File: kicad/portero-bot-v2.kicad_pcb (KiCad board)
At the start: 2 copper layers, 117.5 x 104.5 mm, 75 parts, among them J1 DC005, J2 HR911105A, J3 USB Micro B, J4 KF301-2P, J5 KF301-2P, J6 KF301-2P, J7 Pin Header 01x04 2.54mm Verti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, K1 SRD-05VDC-SL-C, K2 SRD-05VDC-SL-C, K3 SRD-05VDC-SL-C, Q1 2N2222A, Q2 2N2222A, Q3 2N2222A, SW1 KH-6X6X5H-STM, SW2 KH-6X6X5H-STM, U1 ESP32-WROOM-32E-N16, U2 W5500, U3 CH340C, U4 MP2307DN-HW-LF-Z, U5 MP2307DN-HW-LF-Z, Y1 NX3225GA-25MHZ-STD-CRG-2

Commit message: fix(pcb): conectar J3 USB Micro 5V/GND + labels LED PWR
- J3.5 (GND): traza manual + fix vías 0mm con 51_fix_via_sizes (scripts 66, 69)
- J3.1 (5V): path U manual F.Cu rodeando obstáculos B.Cu (RELAY3_COIL_LOW + BST_3V3)
- Eliminadas 3 vías duplicadas en (116, 144.5) — bug interactive router (script 68)
- Labels silkscreen "PWR 3V3" cerca de LED1 + "PWR 5V" cerca de LED5 (script 67)
- DRC: 0 errors, 0 unconnected, 0 footprint errors — JLCPCB-ready

Co-Authored-By: Claude Opus 4.7 <noreply@anthropic.com>
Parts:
- moved J3 6.25 mm to (113.4, 148.0)
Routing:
- net 5V: track 254.4 -> 267.4 mm, vias 4 -> 5
- net GND: track 493.4 -> 505.6 mm, vias 4 -> 5
- net USB_D_N: track 35.4 -> 41.8 mm
- net BST_3V3: track 71.3 -> 65.0 mm
- net USB_D_P: track 34.3 -> 36.2 mm
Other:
- board text added: "PWR 3V3"
- board text added: "PWR 5V"
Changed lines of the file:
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@@
 	(footprint "Connector_USB:USB_Micro-B_Wuerth_614105150721_Vertical"
 		(layer "F.Cu")
-		(at 112.775 141.78)
+		(at 113.4 148)
 		(descr "USB Micro-B receptacle, through-hole, vertical, http://katalog.we-online.de/em/datasheet/614105150721.pdf")
 		(tags "usb micro receptacle vertical")
@@
 		)
 	)
+	(gr_text "PWR 3V3"
+		(at 73.5 127 90)
+		(layer "F.SilkS")
+		(effects
+			(font
+				(size 1 1)
+				(thickness 0.15)
+			)
+			(justify left)
+		)
+	)
+	(gr_text "PWR 5V"
+		(at 73.5 135.5 90)
+		(layer "F.SilkS")
+		(effects
+			(font
+				(size 1 1)
+				(thickness 0.15)
+			)
+			(justify left)
+		)
+	)
 	(gr_text "ENTRADA"
 		(at 77 67 90)
@@
 	)
 	(segment
+		(start 125.542 149.958)
+		(end 125.542 143.542)
+		(width 0.25)
+		(layer "F.Cu")
+		(net "5V")
+	)
+	(segment
 		(start 84.1 107.3)
 		(end 92.305 107.3)
@@
 	)
 	(segment
-		(start 126.4599 142.6241)
-		(end 125.2466 143.8374)
-		(width 0.25)
-		(layer "F.Cu")
-		(net "5V")
-	)
-	(segment
-		(start 144.2865 145.6735)
-		(end 143.5001 144.8871)
-		(width 0.25)
-		(layer "F.Cu")
-		(net "5V")
-	)
-	(segment
 		(start 153.37 129.92)
 		(end 153.37 132.87)
@@
 	)
 	(segment
-		(start 113.5202 143.8374)
-		(end 112.775 143.0922)
+		(start 143.5001 144.8871)
+		(end 144.2865 145.6735)
 		(width 0.25)
 		(layer "F.Cu")
@@
 	)
 	(segment
-		(start 125.2466 143.8374)
-		(end 113.5202 143.8374)
+		(start 155.816 136.2796)
+		(end 156.0008 136.0948)
 		(width 0.25)
 		(layer "F.Cu")
@@
 	)
 	(segment
-		(start 155.816 136.2796)
-		(end 156.0008 136.0948)
+		(start 156.0008 135.5008)
+		(end 153.37 132.87)
 		(width 0.25)
 		(layer "F.Cu")
@@
 	)
 	(segment
-		(start 156.0008 135.5008)
-		(end 153.37 132.87)
+		(start 141.9984 142.6241)
+		(end 143.5001 144.1258)
+		(width 0.25)
+		(layer "F.Cu")
+		(net "5V")
+	)
+	(segment
+		(start 113.4 138.6)
+		(end 113.5 138.5)
 		(width 0.25)
 		(layer "F.Cu")
@@
 	)
 	(segment
+		(start 113.4 150.4)
+		(end 113.5 150.5)
+		(width 0.25)
+		(layer "F.Cu")
+		(net "5V")
+	)
+	(segment
 		(start 116.9286 127.724)
 		(end 119.1675 127.724)
@@
 	)
 	(segment
-		(start 143.5001 144.8871)
-		(end 143.5001 144.1258)
+		(start 125.542 143.542)
+		(end 126.4599 142.6241)
 		(width 0.25)
 		(layer "F.Cu")
@@
 	)
 	(segment
-		(start 146.6626 145.6735)
-		(end 144.2865 145.6735)
+		(start 113.4 148)
+		(end 113.4 138.6)
 		(width 0.25)
 		(layer "F.Cu")
@@
 	)
 	(segment
-		(start 143.5001 144.1258)
-		(end 141.9984 142.6241)
+		(start 113.5 150.5)
+		(end 125 150.5)
 		(width 0.25)
 		(layer "F.Cu")
@@
 	)
 	(segment
-		(start 153.8296 136.2796)
-		(end 153.8296 138.5065)
+		(start 126.4599 142.6241)
+		(end 141.9984 142.6241)
 		(width 0.25)
 		(layer "F.Cu")
@@
 	)
 	(segment
+		(start 125 150.5)
+		(end 125.542 149.958)
+		(width 0.25)
+		(layer "F.Cu")
+		(net "5V")
+	)
+	(segment
+		(start 143.5001 144.1258)
+		(end 143.5001 144.8871)
+		(width 0.25)
+		(layer "F.Cu")
+		(net "5V")
+	)
+	(segment
 		(start 121.5 113.6857)
 		(end 121.5 112.7)
@@
 	)
 	(segment
-		(start 112.775 143.0922)
-		(end 112.775 141.78)
+		(start 113.4 148)
+		(end 113.4 150.4)
 		(width 0.25)
 		(layer "F.Cu")
@@
 	)
 	(segment
-		(start 153.8296 138.5065)
-		(end 146.6626 145.6735)
-		(width 0.25)
-		(layer "F.Cu")
-		(net "5V")
-	)
-	(segment
 		(start 98.575 117.82)
 		(end 98.575 113.57)
@@
 	)
 	(segment
+		(start 144.2865 145.6735)
+		(end 146.6626 145.6735)
+		(width 0.25)
+		(layer "F.Cu")
+		(net "5V")
+	)
+	(segment
 		(start 106.7282 112.6851)
 		(end 106.7283 112.685)
@@
 	)
 	(segment
-		(start 141.9984 142.6241)
-		(end 126.4599 142.6241)
+		(start 153.8296 138.5065)
+		(end 153.8296 136.2796)
+		(width 0.25)
+		(layer "F.Cu")
+		(net "5V")
+	)
+	(segment
+		(start 146.6626 145.6735)
+		(end 153.8296 138.5065)
 		(width 0.25)
 		(layer "F.Cu")
@@
 	)
 	(via
+		(at 113.5 138.5)
+		(size 0.5)
+		(drill 0.3)
+		(layers "F.Cu" "B.Cu")
+		(net "5V")
+	)
+	(via
 		(at 114.6012 135.8835)
 		(size 0.6)
@@
 	)
 	(segment
+		(start 113.5 138.5)
+		(end 113.5 137.0645)
+		(width 0.2)
+		(layer "B.Cu")
+		(net "5V")
+	)
+	(segment
 		(start 101.35 81.95)
 		(end 101.35 98.9)
@@
 	)
 	(segment
+		(start 113.5 137.0645)
+		(end 113.4601 137.0246)
+		(width 0.2)
+		(layer "B.Cu")
+		(net "5V")
+	)
+	(segment
 		(start 113.4601 137.0246)
 		(end 114.6012 135.8835)
@@
 	)
 	(segment
-		(start 112.775 141.78)
-		(end 112.775 137.0246)
-		(width 0.25)
-		(layer "B.Cu")
-		(net "5V")
-	)
-	(segment
 		(start 108.2275 133.2538)
 		(end 108.3149 133.3412)
@@
 	)
 	(segment
+		(start 126.405 134.49)
+		(end 126.01 134.49)
+		(width 0.25)
+		(layer "F.Cu")
+		(net "GND")
+	)
+	(segment
 		(start 121.5 125.25)
 		(end 121.5 124.7916)
@@
 	)
 	(segment
+		(start 126.01 134.49)
+		(end 116 144.5)
+		(width 0.25)
+		(layer "F.Cu")
+		(net "GND")
+	)
+	(segment
 		(start 148.025 125.22)
 		(end 146.12 127.125)
@@
 	)
 	(via
+		(at 116 144.5)
+		(size 0.5)
+		(drill 0.3)
+		(layers "F.Cu" "B.Cu")
+		(net "GND")
+	)
+	(via
 		(at 113.9682 134.4766)
 		(size 0.6)
@@
 	)
 	(segment
+		(start 116 148)
+		(end 116 144.5)
+		(width 0.25)
+		(layer "B.Cu")
+		(net "GND")
+	)
+	(segment
 		(start 153.4683 100.5117)
 		(end 153.4683 119.0333)
@@
 	)
 	(segment
-		(start 115.375 141.78)
-		(end 115.375 135.8834)
-		(width 0.25)
-		(layer "B.Cu")
-		(net "GND")
-	)
-	(segment
 		(start 155.13 98.85)
 		(end 153.4683 100.5117)
@@
 	)
 	(segment
-		(start 145.55 136.25)
-		(end 131.2756 136.25)
+		(start 114 149.05)
+		(end 114.05 149)
+		(width 0.25)
+		(layer "F.Cu")
+		(net "USB_D_N")
+	)
+	(segment
+		(start 123.5 150)
+		(end 114 150)
 		(width 0.25)
 		(layer "F.Cu")
@@
 	)
 	(segment
-		(start 114.1041 143.4591)
-		(end 113.425 142.78)
+		(start 145.55 136.25)
+		(end 131.2756 136.25)
+		(width 0.25)
+		(layer "F.Cu")
+		(net "USB_D_N")
+	)
+	(segment
+		(start 124.0665 149.4335)
+		(end 123.5 150)
+		(width 0.25)
+		(layer "F.Cu")
+		(net "USB_D_N")
+	)
+	(segment
+		(start 114 150)
+		(end 114 149.05)
 		(width 0.25)
 		(layer "F.Cu")
@@
 	(segment
 		(start 124.0665 143.4591)
-		(end 114.1041 143.4591)
+		(end 124.0665 149.4335)
 		(width 0.25)
 		(layer "F.Cu")
@@
 	)
 	(segment
-		(start 114.075 141.78)
-		(end 119.5632 136.2918)
+		(start 129.7486 134.98)
+		(end 145.55 134.98)
 		(width 0.25)
 		(layer "F.Cu")
@@
 	)
 	(segment
-		(start 128.4368 136.2918)
-		(end 129.7486 134.98)
+		(start 117.5 145.2)
+		(end 119.5286 145.2)
 		(width 0.25)
 		(layer "F.Cu")
@@
 	)
 	(segment
-		(start 119.5632 136.2918)
-		(end 128.4368 136.2918)
+		(start 114.7 148)
+		(end 117.5 145.2)
 		(width 0.25)
 		(layer "F.Cu")
@@
 	)
 	(segment
-		(start 129.7486 134.98)
-		(end 145.55 134.98)
+		(start 119.5286 145.2)
+		(end 129.7486 134.98)
 		(width 0.25)
 		(layer "F.Cu")
@@
 	)
 	(segment
-		(start 116.324 142.1119)
-		(end 114.9777 143.4582)
-		(width 0.25)
-		(layer "B.Cu")
-		(net "BST_3V3")
-	)
-	(segment
-		(start 112.0597 142.3623)
-		(end 112.0597 141.1093)
-		(width 0.25)
-		(layer "B.Cu")
-		(net "BST_3V3")
-	)
-	(segment
-		(start 113.1556 143.4582)
-		(end 112.0597 142.3623)
+		(start 116.324 139)
+		(end 109.9504 139)
 		(width 0.25)
 		(layer "B.Cu")
@@
 	(segment
 		(start 116.324 138.9386)
-		(end 116.324 142.1119)
-		(width 0.25)
-		(layer "B.Cu")
-		(net "BST_3V3")
-	)
-	(segment
-		(start 114.9777 143.4582)
-		(end 113.1556 143.4582)
+		(end 116.324 139)
 		(width 0.25)
 		(layer "B.Cu")
@@
 	)
 	(segment
-		(start 112.0597 141.1093)
+		(start 109.9504 139)
 		(end 107.1545 136.2041)
 		(width 0.25)

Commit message: fix(pcb): power tree — U4/U5 EN flotantes + VIN_BUCK huerfano
Bugs criticos en source EDIF -> master.json:
- 'Net 2' (auto-generated) era input del U5 buck (3.3V) en lugar de VIN_BUCK
- U4 (5V buck) tenia VIN_BUCK aislado: solo conectaba a U4.2/U4.7, sin source
- U4.6 (EN) y U5.6 (EN) flotantes -> MP2307 puede no arrancar

Fix:
- Net 2 + VIN_BUCK fusionados en un solo rail VIN_BUCK
- F1.2 (fuse output) ahora alimenta ambos bucks (U4 + U5)
- U4.6/U5.6 (EN) tied a su VIN respectivo con track corto F.Cu (1.27mm)
- Bridge B.Cu entre rails previamente aislados (0.67mm)

DRC: 0 errors, 0 unconnected, 0 footprint errors
Verificado: F1.2 + U4.2/6/7 + U5.2/6/7 todos en mismo net VIN_BUCK (44 items)

Co-Authored-By: Claude Opus 4.7 <noreply@anthropic.com>
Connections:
- F1 pad 2: Net 2 -> VIN_BUCK
- U4 pad 6: (no net) -> VIN_BUCK
- U5 pad 2: Net 2 -> VIN_BUCK
- U5 pad 6: (no net) -> VIN_BUCK
- U5 pad 7: Net 2 -> VIN_BUCK
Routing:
- net VIN_BUCK: track 14.2 -> 61.3 mm, vias 4 -> 8
- net Net 2: track 43.9 -> 0.00 mm, vias 4 -> 0

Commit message: fix(pcb): C22/C23 bootstrap caps 100uF -> 100nF (datasheet MP2307)
Bug: C22/C23 (bootstrap caps de MP2307) tenian valor 100uF del netlist Flux.
Datasheet MP2307 requiere BST cap = 100nF ceramico. 100uF impide switching correcto.
Fix BOM-only (footprint 1210 acepta ambos valores).

Scripts 72-74 son intentos fallidos de agregar C18/C19/C24 (deferidos a V3):
- Zona U4/U5/J7 muy congestionada para agregar componentes sin re-layout
- Sin input caps, MP2307 funcional con C16/C17 (100uF output) + L1 + F1 como filter chain
- Para 24/7: ESP32 brownout detector + WiFi/Ethernet redundancy compensan limitacion
- Firmware debe secuencializar activacion relays (no simultaneos)

DRC: 0 errors, 0 unconnected, 0 footprint errors — JLCPCB-ready

Co-Authored-By: Claude Opus 4.7 <noreply@anthropic.com>
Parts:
- C22, C23: value 100uF -> 100nF
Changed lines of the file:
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@@
 			)
 		)
-		(property "Value" "100uF"
+		(property "Value" "100nF"
 			(at 0 2.3 0)
 			(layer "F.Fab")
@@
 			)
 		)
-		(property "Value" "100uF"
+		(property "Value" "100nF"
 			(at 0 2.3 0)
 			(layer "F.Fab")

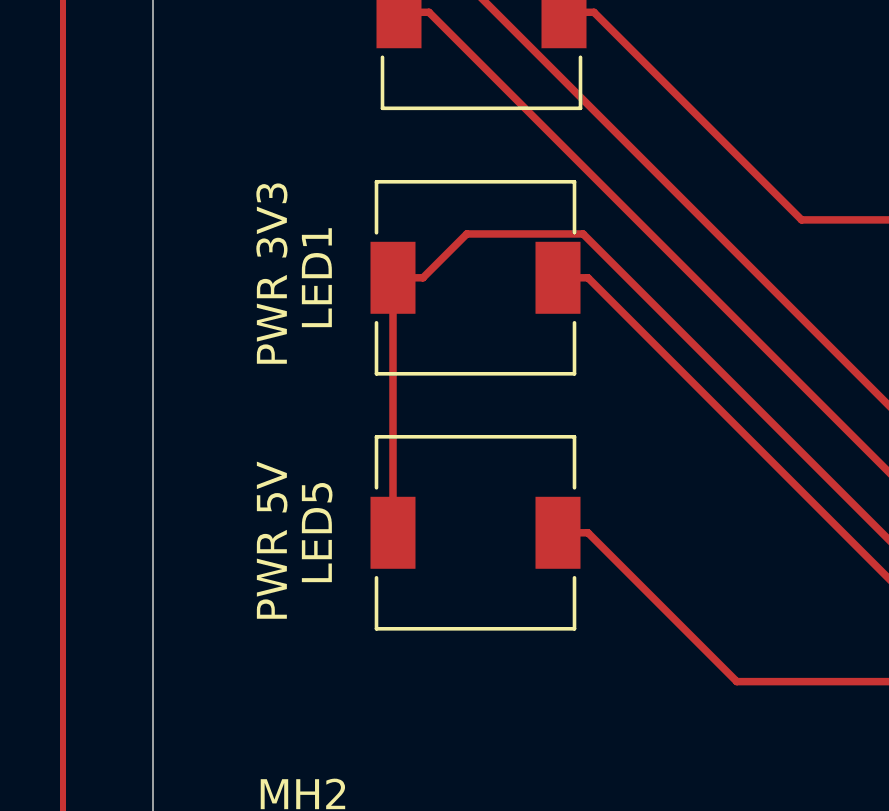
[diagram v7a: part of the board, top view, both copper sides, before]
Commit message: fix(pcb): LED1/LED5 footprint inductor -> LED_0603 + export Gerbers JLCPCB
Bug: LED1 (0603GBD0790S01) y LED5 (LTST-C190KSKT) tenian footprint
L_6.3x6.3_H3 (inductor 6.3x6.3mm con pad gap 5.5mm) heredado del netlist Flux.
LEDs reales son chip 0603 con pad gap 0.8mm -> JLCPCB Assembly habria rechazado.

Fix: reemplazo a LED_0603_1608Metric, conservando posicion (80.25,124) y (80.25,132.5).
3 tracks LED1 + 2 tracks LED5 re-routeados a nuevos pad positions.
DRC: 0 errors, 0 unconnected, 0 footprint.

Outputs JLCPCB-ready en kicad/gerbers/:
- 9 layers Gerber (F/B Cu/Mask/Silkscreen/Paste + Edge)
- PTH + NPTH drill files
- portero-bot-v2-GERBERS.zip (49KB)
- BOM CSV (34 grupos, 71 componentes, LCSC# vacios - pendiente llenar)
- CPL/Pick-and-place CSV

Co-Authored-By: Claude Opus 4.7 <noreply@anthropic.com>
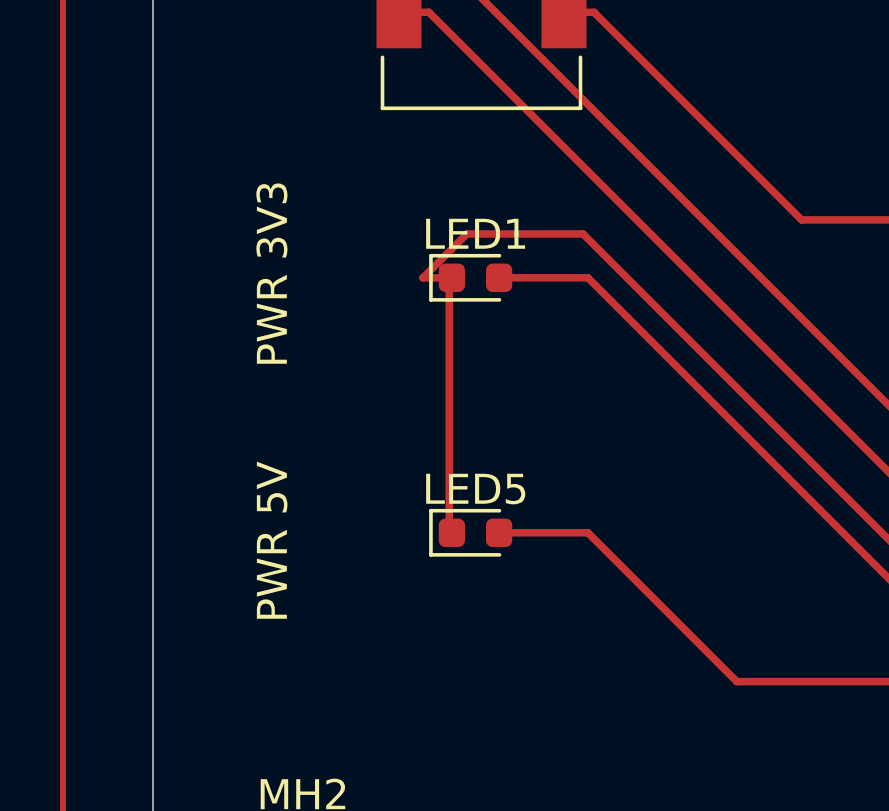
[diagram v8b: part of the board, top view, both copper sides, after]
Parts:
- LED1, LED5: footprint Inductor_SMD:L_6.3x6.3_H3 -> LED_0603_1608Metric
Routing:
- net LED_3V3_PWR: track 43.9 -> 45.8 mm
- net LED5_5V_IND: track 45.8 -> 47.7 mm
